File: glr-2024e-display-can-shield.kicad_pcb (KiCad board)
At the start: 2 copper layers, 46 x 90 mm, 11 parts, among them CN12 Conn_02x08_Odd_Even, CN6 Conn_01x08, CN8 Conn_01x06, IC1 L9615D013TR, IC2 LF80CDT-TR, J1 Screw_Terminal_01x04, J2 Screw_Terminal_01x08

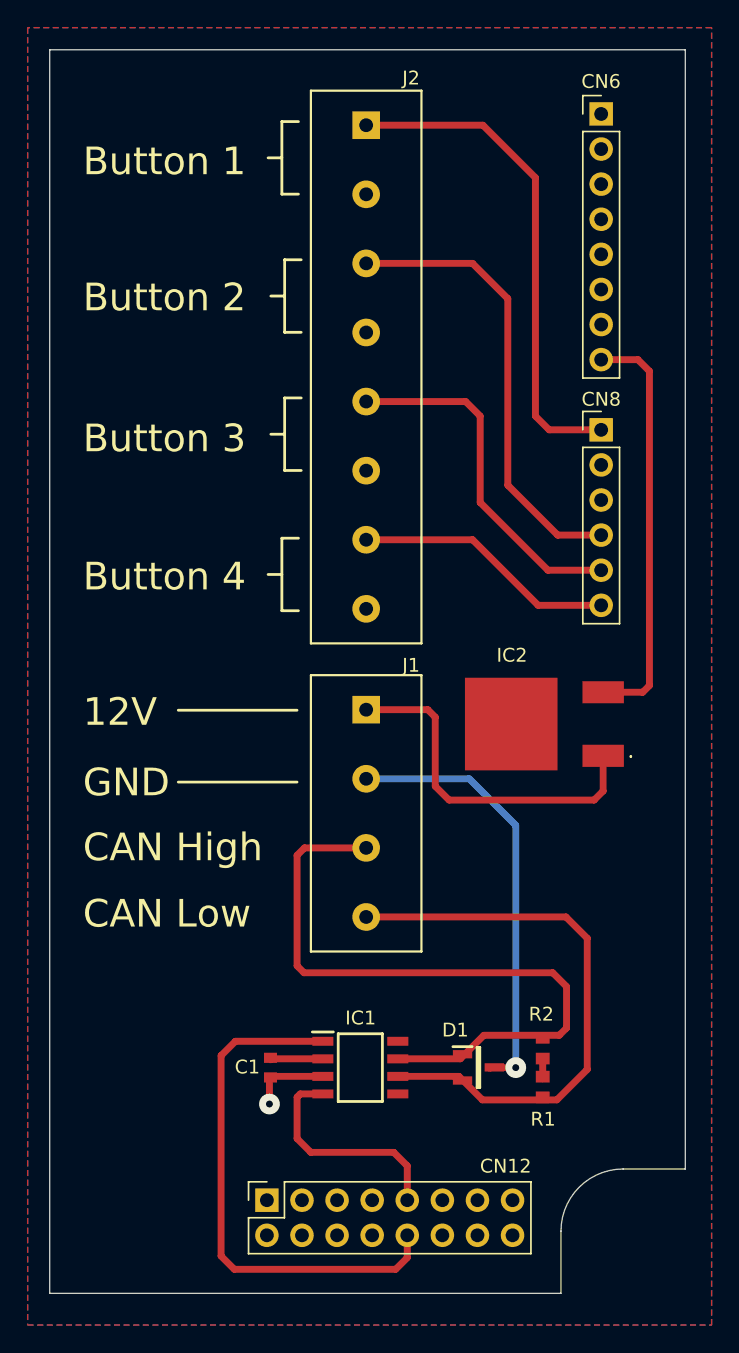
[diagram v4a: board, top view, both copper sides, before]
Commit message: fix capacitor connection
fix silk on terminal
add output folder

Co-Authored-By: wallalex0 <97884125+wallalex0@users.noreply.github.com>
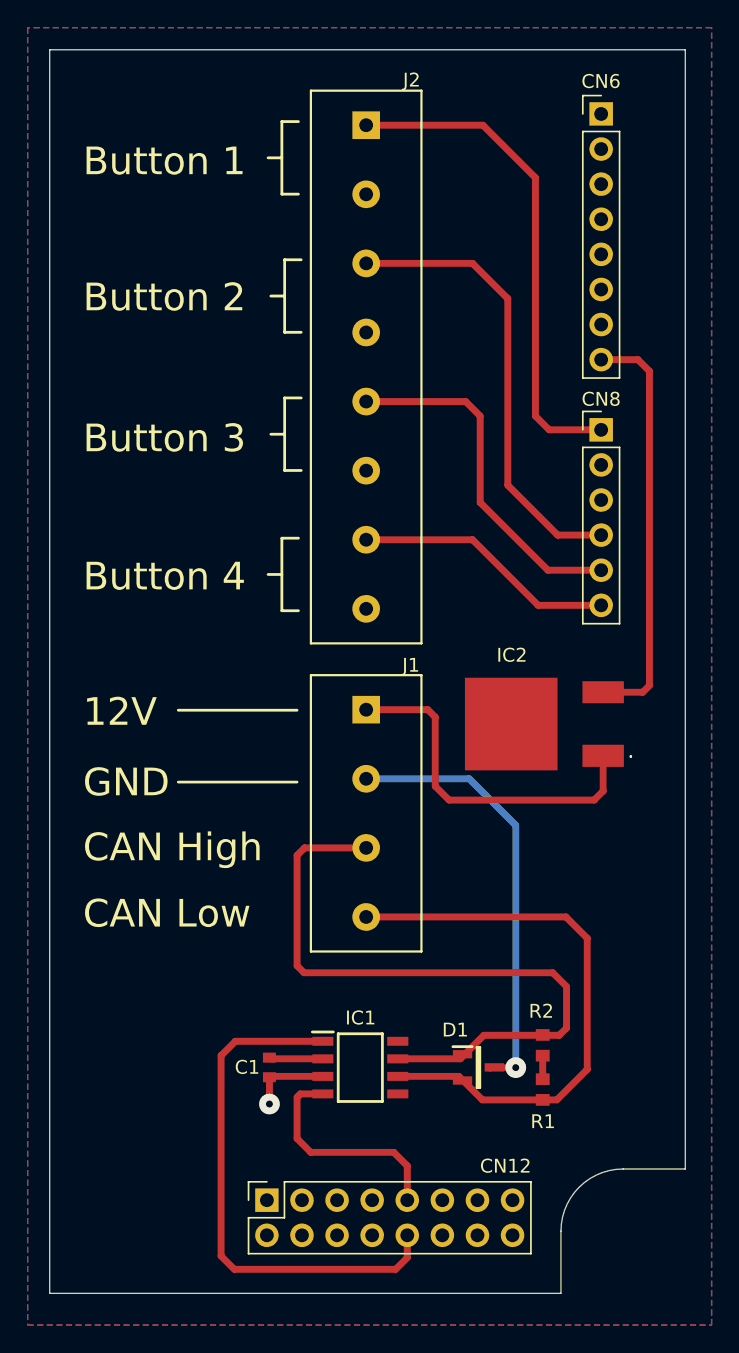
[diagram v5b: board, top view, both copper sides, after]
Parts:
- J1: footprint GLR_KiCAD_Library:WECO-950-FB-04 -> GLR_KiCad_Library:WECO-950-FB-04
- J2: footprint GLR_KiCAD_Library:WECO-950-FB-08 -> GLR_KiCad_Library:WECO-950-FB-08
- moved R2 0.21 mm to (153.3, 117.2)
- moved R1 0.18 mm to (153.3, 120.5)
- moved C1 0.08 mm to (133.5, 118.8), turned to 90 degrees
